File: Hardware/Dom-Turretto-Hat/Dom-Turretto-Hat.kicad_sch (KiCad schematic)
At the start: 4 parts

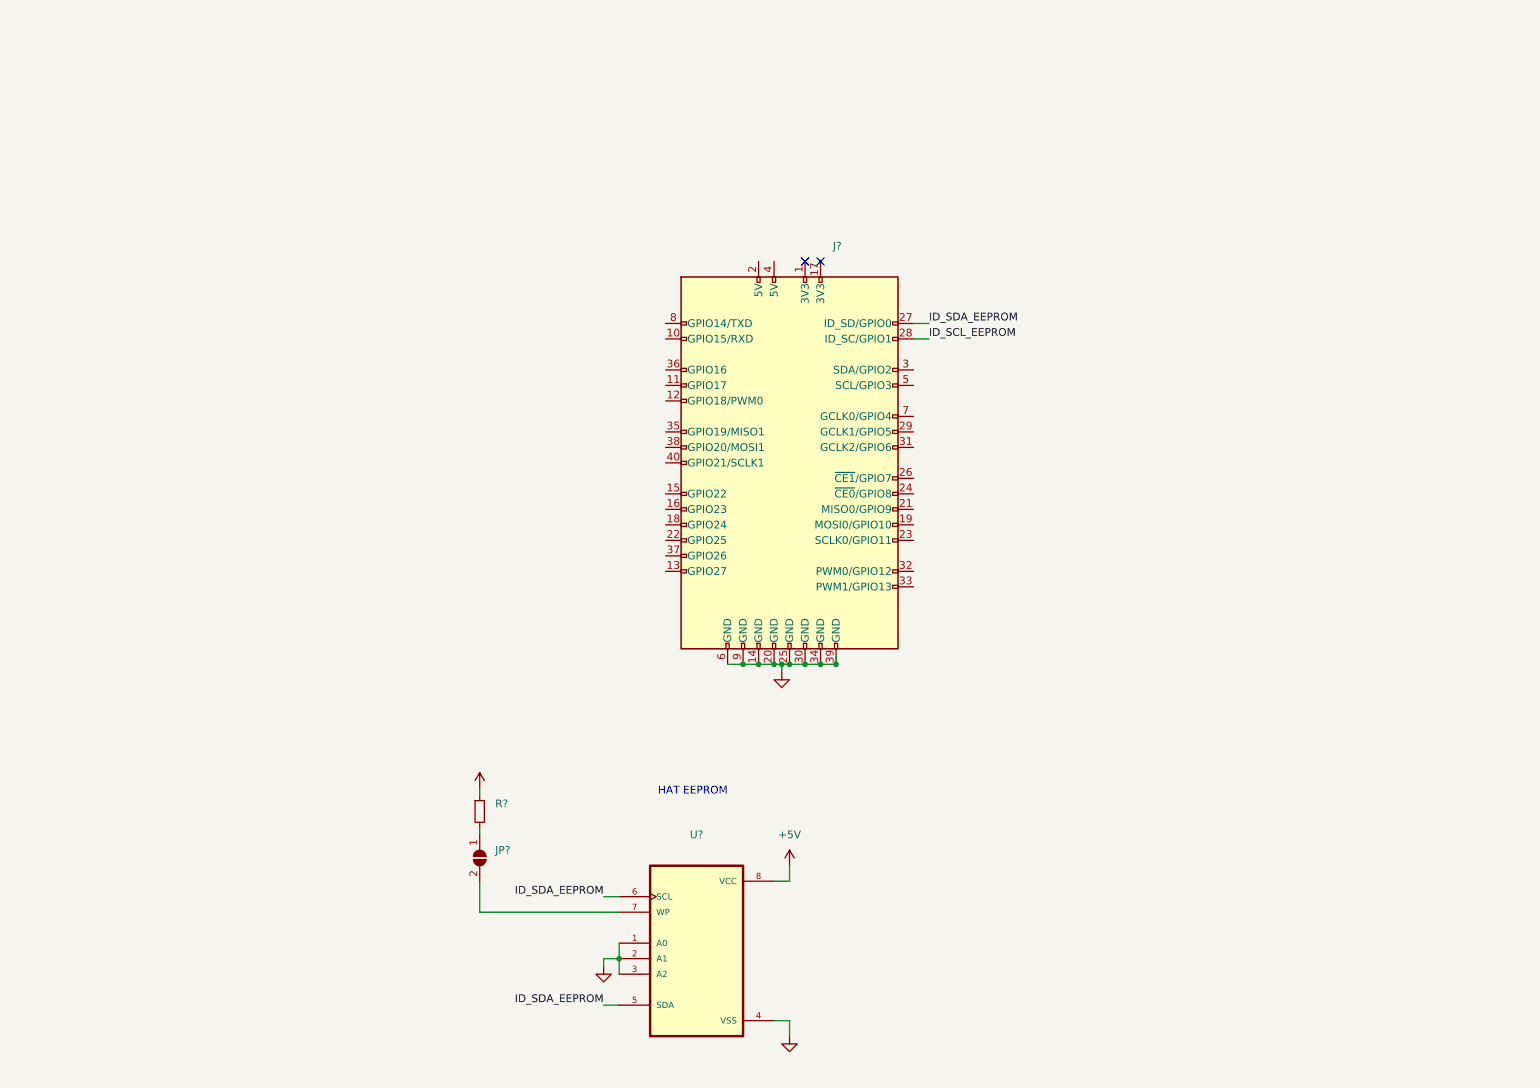
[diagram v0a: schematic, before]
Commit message: Add GPS
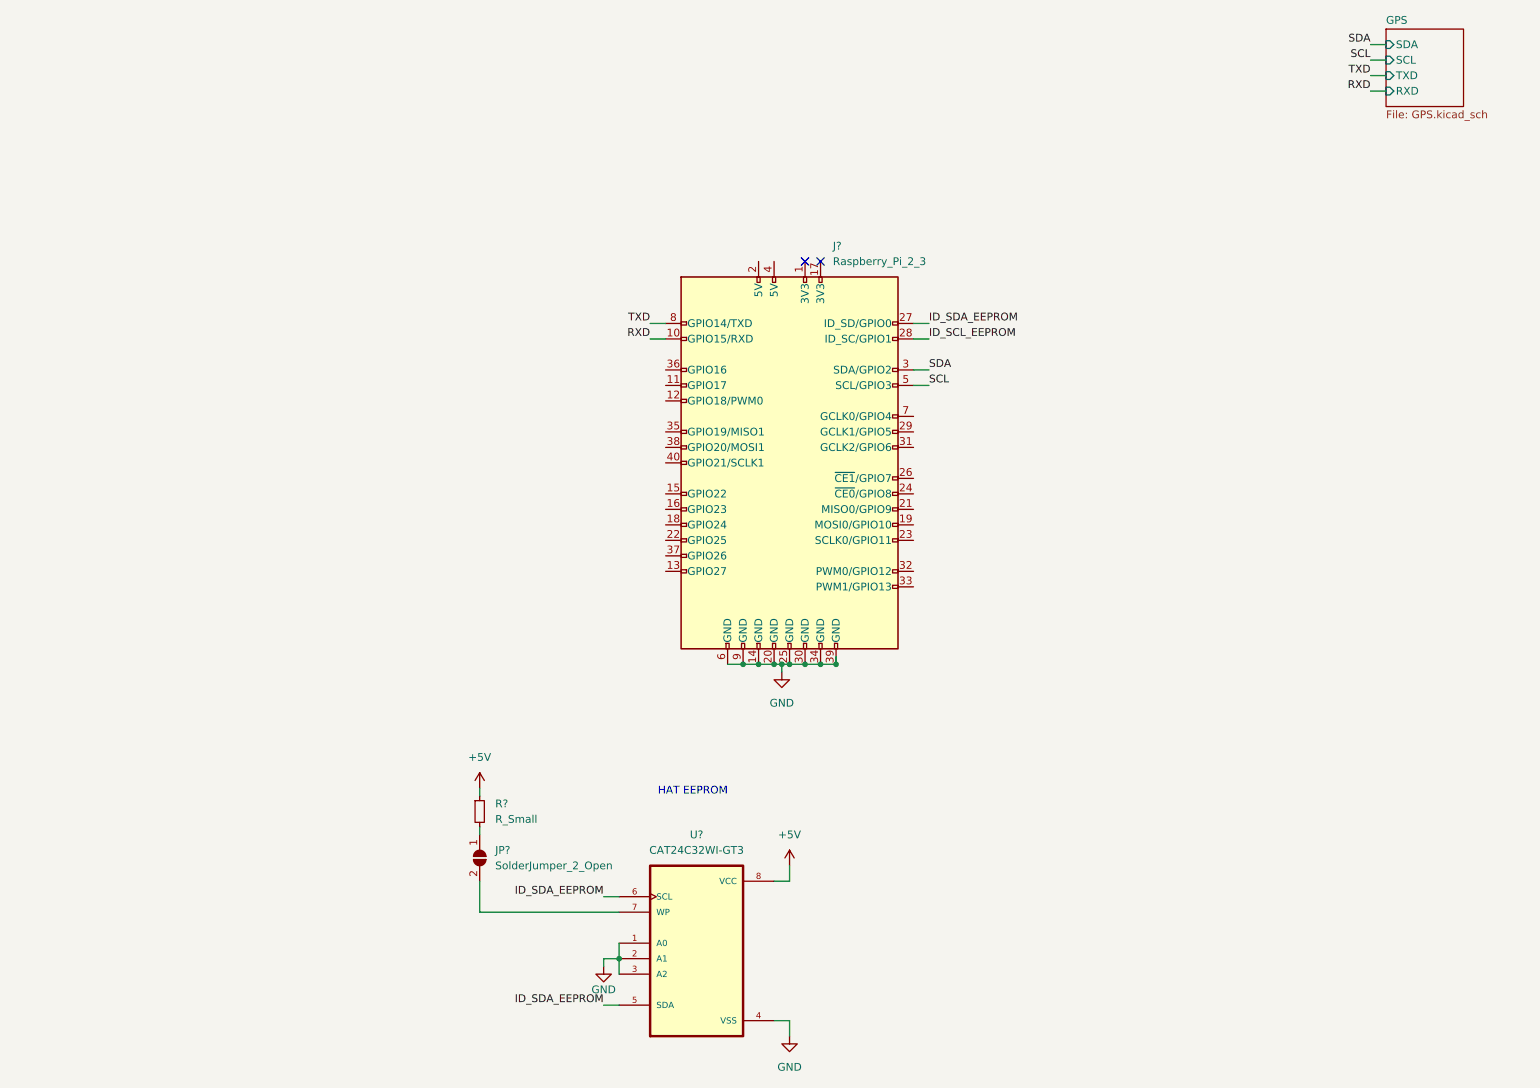
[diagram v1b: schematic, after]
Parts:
- J?: value (none) -> Raspberry_Pi_2_3; footprint (none) -> Connector_PinSocket_2.54mm:PinSocket_2x20_P2.54mm_Vertical
- JP?: value (none) -> SolderJumper_2_Open
- R?: value (none) -> R_Small
- U?: value (none) -> CAT24C32WI-GT3; footprint (none) -> SOIC127P600X175-8N
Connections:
- net RXD: now reaches J?.10 (GPIO15/RXD)
- net SDA: now reaches J?.3 (SDA/GPIO2)
- net SCL: now reaches J?.5 (SCL/GPIO3)
- net TXD: now reaches J?.8 (GPIO14/TXD)
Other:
- added sheet GPS (GPS.kicad_sch)
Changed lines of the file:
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@@
+    (stroke (width 0) (type default) (color 0 0 0 0))
+  )
+  (wire (pts (xy 248.92 30.48) (xy 251.46 30.48))
     (stroke (width 0) (type default) (color 0 0 0 0))
   )
@@
     (stroke (width 0) (type default) (color 0 0 0 0))
   )
+  (wire (pts (xy 130.81 73.66) (xy 133.35 73.66))
+    (stroke (width 0) (type default) (color 0 0 0 0))
+  )
   (wire (pts (xy 173.99 76.2) (xy 176.53 76.2))
     (stroke (width 0) (type default) (color 0 0 0 0))
@@
     (stroke (width 0) (type default) (color 0 0 0 0))
   )
+  (wire (pts (xy 173.99 83.82) (xy 176.53 83.82))
+    (stroke (width 0) (type default) (color 0 0 0 0))
+  )
+  (wire (pts (xy 248.92 27.94) (xy 251.46 27.94))
+    (stroke (width 0) (type default) (color 0 0 0 0))
+  )
   (wire (pts (xy 151.13 187.96) (xy 153.67 187.96))
     (stroke (width 0) (type default) (color 0 0 0 0))
   )
+  (wire (pts (xy 130.81 76.2) (xy 133.35 76.2))
+    (stroke (width 0) (type default) (color 0 0 0 0))
+  )
   (wire (pts (xy 123.19 177.8) (xy 123.19 179.07))
     (stroke (width 0) (type default) (color 0 0 0 0))
@@
     (stroke (width 0) (type default) (color 0 0 0 0))
   )
+  (wire (pts (xy 248.92 35.56) (xy 251.46 35.56))
+    (stroke (width 0) (type default) (color 0 0 0 0))
+  )
   (wire (pts (xy 102.87 165.1) (xy 102.87 170.18))
     (stroke (width 0) (type default) (color 0 0 0 0))
@@
     (stroke (width 0) (type default) (color 0 0 0 0))
   )
+  (wire (pts (xy 173.99 81.28) (xy 176.53 81.28))
+    (stroke (width 0) (type default) (color 0 0 0 0))
+  )
   (wire (pts (xy 173.99 73.66) (xy 176.53 73.66))
     (stroke (width 0) (type default) (color 0 0 0 0))
   )
   (wire (pts (xy 153.67 187.96) (xy 153.67 190.5))
+    (stroke (width 0) (type default) (color 0 0 0 0))
+  )
+  (wire (pts (xy 248.92 33.02) (xy 251.46 33.02))
     (stroke (width 0) (type default) (color 0 0 0 0))
   )
@@
     (effects (font (size 1.27 1.27)) (justify left bottom))
   )
+  (label "SDA" (at 176.53 81.28 0)
+    (effects (font (size 1.27 1.27)) (justify left bottom))
+  )
+  (label "TXD" (at 248.92 33.02 180)
+    (effects (font (size 1.27 1.27)) (justify right bottom))
+  )
   (label "ID_SDA_EEPROM" (at 176.53 73.66 0)
     (effects (font (size 1.27 1.27)) (justify left bottom))
   )
+  (label "SDA" (at 248.92 27.94 180)
+    (effects (font (size 1.27 1.27)) (justify right bottom))
+  )
   (label "ID_SDA_EEPROM" (at 123.19 167.64 180)
     (effects (font (size 1.27 1.27)) (justify right bottom))
   )
+  (label "SCL" (at 176.53 83.82 0)
+    (effects (font (size 1.27 1.27)) (justify left bottom))
+  )
   (label "ID_SDA_EEPROM" (at 123.19 185.42 180)
     (effects (font (size 1.27 1.27)) (justify right bottom))
   )
+  (label "RXD" (at 248.92 35.56 180)
+    (effects (font (size 1.27 1.27)) (justify right bottom))
+  )
+  (label "TXD" (at 130.81 73.66 180)
+    (effects (font (size 1.27 1.27)) (justify right bottom))
+  )
+  (label "RXD" (at 130.81 76.2 180)
+    (effects (font (size 1.27 1.27)) (justify right bottom))
+  )
+  (label "SCL" (at 248.92 30.48 180)
+    (effects (font (size 1.27 1.27)) (justify right bottom))
+  )
   (symbol (lib_id "power:GND") (at 152.4 130.81 0) (unit 1)
     (in_bom yes) (on_board yes) (fields_autoplaced)
@@
       (effects (font (size 1.27 1.27)) hide)
     )
-    (property "Value" "" (id 1) (at 152.4 135.89 0))
+    (property "Value" "GND" (id 1) (at 152.4 135.89 0))
     (property "Footprint" "" (id 2) (at 152.4 130.81 0)
       (effects (font (size 1.27 1.27)) hide)
@@
     (in_bom yes) (on_board yes) (fields_autoplaced)
     (property "Reference" "U?" (id 0) (at 138.43 157.48 0))
-    (property "Value" "" (id 1) (at 138.43 160.02 0))
-    (property "Footprint" "" (id 2) (at 138.43 175.26 0)
+    (property "Value" "CAT24C32WI-GT3" (id 1) (at 138.43 160.02 0))
+    (property "Footprint" "SOIC127P600X175-8N" (id 2) (at 138.43 175.26 0)
       (effects (font (size 1.27 1.27)) (justify left bottom) hide)
     )
@@
       (effects (font (size 1.27 1.27)) hide)
     )
-    (property "Value" "" (id 1) (at 102.87 144.78 0))
+    (property "Value" "+5V" (id 1) (at 102.87 144.78 0))
     (property "Footprint" "" (id 2) (at 102.87 149.86 0)
       (effects (font (size 1.27 1.27)) hide)
@@
       (effects (font (size 1.27 1.27)) (justify left))
     )
-    (property "Value" "" (id 1) (at 160.7694 63.5 0)
-      (effects (font (size 1.27 1.27)) (justify left))
-    )
-    (property "Footprint" "" (id 2) (at 153.67 96.52 0)
+    (property "Value" "Raspberry_Pi_2_3" (id 1) (at 160.7694 63.5 0)
+      (effects (font (size 1.27 1.27)) (justify left))
+    )
+    (property "Footprint" "Connector_PinSocket_2.54mm:PinSocket_2x20_P2.54mm_Vertical" (id 2) (at 153.67 96.52 0)
       (effects (font (size 1.27 1.27)) hide)
     )
@@
       (effects (font (size 1.27 1.27)) (justify left))
     )
-    (property "Value" "" (id 1) (at 105.41 162.5599 90)
+    (property "Value" "SolderJumper_2_Open" (id 1) (at 105.41 162.5599 90)
       (effects (font (size 1.27 1.27)) (justify left))
     )
@@
       (effects (font (size 1.27 1.27)) hide)
     )
-    (property "Value" "" (id 1) (at 153.67 195.58 0))
+    (property "Value" "GND" (id 1) (at 153.67 195.58 0))
     (property "Footprint" "" (id 2) (at 153.67 190.5 0)
       (effects (font (size 1.27 1.27)) hide)
@@
       (effects (font (size 1.27 1.27)) hide)
     )
-    (property "Value" "" (id 1) (at 123.19 182.88 0))
+    (property "Value" "GND" (id 1) (at 123.19 182.88 0))
     (property "Footprint" "" (id 2) (at 123.19 179.07 0)
       (effects (font (size 1.27 1.27)) hide)
@@
       (effects (font (size 1.27 1.27)) (justify left))
     )
-    (property "Value" "" (id 1) (at 105.41 154.9399 0)
+    (property "Value" "R_Small" (id 1) (at 105.41 154.9399 0)
       (effects (font (size 1.27 1.27)) (justify left))
     )
@@
     (pin "1")
     (pin "2")
+  )
+  (sheet (at 251.46 25.4) (size 12.7 12.7) (fields_autoplaced)
+    (stroke (width 0.1524) (type solid) (color 0 0 0 0))
+    (fill (color 0 0 0 0.0000))
+    (property "Sheet name" "GPS" (id 0) (at 251.46 24.6884 0)
+      (effects (font (size 1.27 1.27)) (justify left bottom))
+    )
+    (property "Sheet file" "GPS.kicad_sch" (id 1) (at 251.46 38.6846 0)
+      (effects (font (size 1.27 1.27)) (justify left top))
+    )
+    (pin "RXD" input (at 251.46 35.56 180)
+      (effects (font (size 1.27 1.27)) (justify left))
+    )
+    (pin "SDA" input (at 251.46 27.94 180)
+      (effects (font (size 1.27 1.27)) (justify left))
+    )
+    (pin "SCL" input (at 251.46 30.48 180)
+      (effects (font (size 1.27 1.27)) (justify left))
+    )
+    (pin "TXD" input (at 251.46 33.02 180)
+      (effects (font (size 1.27 1.27)) (justify left))
+    )
   )
   (sheet_instances
     (path "/" (page "1"))
+    (path "/c8c14f7c-55ef-44f2-9b65-a499409017e1" (page "2"))
   )
   (symbol_instances
@@
       (reference "#PWR?") (unit 1) (value "GND") (footprint "")
     )
+    (path "/c8c14f7c-55ef-44f2-9b65-a499409017e1/451985fb-27af-4988-a96b-5b9018357ef6"
+      (reference "#PWR?") (unit 1) (value "GND") (footprint "")
+    )
     (path "/4bc4c433-f063-4f06-891b-84c21537146f"
       (reference "#PWR?") (unit 1) (value "+5V") (footprint "")
     )
+    (path "/c8c14f7c-55ef-44f2-9b65-a499409017e1/899f9b0d-851b-40b2-95d9-0bf4320cfc7f"
+      (reference "#PWR?") (unit 1) (value "+3V3") (footprint "")
+    )
     (path "/ba4a3115-885a-4dd4-8dfa-d43bc604d1e0"
       (reference "#PWR?") (unit 1) (value "+5V") (footprint "")
     )
+    (path "/c8c14f7c-55ef-44f2-9b65-a499409017e1/d58204f5-4242-4763-8399-6e93946856c1"
+      (reference "#PWR?") (unit 1) (value "GND") (footprint "")
+    )
     (path "/d76951c7-90df-44ef-9dcf-7210c88290e4"
       (reference "#PWR?") (unit 1) (value "GND") (footprint "")
@@
       (reference "#PWR?") (unit 1) (value "GND") (footprint "")
     )
+    (path "/c8c14f7c-55ef-44f2-9b65-a499409017e1/e4566a45-8e06-47ea-a935-fa62dd278c90"
+      (reference "#PWR?") (unit 1) (value "+3V3") (footprint "")
+    )
+    (path "/c8c14f7c-55ef-44f2-9b65-a499409017e1/4fb87244-379d-4e75-94c2-9521bcc0ec81"
+      (reference "C?") (unit 1) (value "10nF") (footprint "Capacitor_SMD:C_0603_1608Metric")
+    )
     (path "/61fae217-e18a-4e68-8630-42cc06a8ba2f"
       (reference "J?") (unit 1) (value "Raspberry_Pi_2_3") (footprint "Connector_PinSocket_2.54mm:PinSocket_2x20_P2.54mm_Vertical")
     )
+    (path "/c8c14f7c-55ef-44f2-9b65-a499409017e1/6a180251-fad0-4435-9a6c-41f5e820bcf1"
+      (reference "J?") (unit 1) (value "Conn_Coaxial") (footprint "Connector_Coaxial:SMA_Molex_73251-1153_EdgeMount_Horizontal")
+    )
     (path "/a4265e2c-06a9-41da-b42d-91d87bbe6b18"
       (reference "JP?") (unit 1) (value "SolderJumper_2_Open") (footprint "")
     )
+    (path "/c8c14f7c-55ef-44f2-9b65-a499409017e1/d6c763e2-1952-4281-9868-501fafa3b154"
+      (reference "L?") (unit 1) (value "27nH") (footprint "Inductor_SMD:L_0603_1608Metric")
+    )
+    (path "/c8c14f7c-55ef-44f2-9b65-a499409017e1/8a505506-ea00-4e73-916e-6375c9e26bd9"
+      (reference "R?") (unit 1) (value "10") (footprint "Resistor_SMD:R_0603_1608Metric")
+    )
+    (path "/c8c14f7c-55ef-44f2-9b65-a499409017e1/d53051b6-ebe9-4558-9887-00e35561baeb"
+      (reference "R?") (unit 1) (value "10K") (footprint "Resistor_SMD:R_0603_1608Metric")
+    )
     (path "/e3cbd370-7c22-4222-878e-9ad9b35baaf2"
       (reference "R?") (unit 1) (value "R_Small") (footprint "")
@@
       (reference "U?") (unit 1) (value "CAT24C32WI-GT3") (footprint "SOIC127P600X175-8N")
     )
-  )
+    (path "/c8c14f7c-55ef-44f2-9b65-a499409017e1/5c054c83-012c-4e45-901b-5550fc59a449"
+      (reference "U?") (unit 1) (value "MAX-M8Q") (footprint "RF_GPS:ublox_MAX")
+    )
+  )

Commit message: Add power circuitry
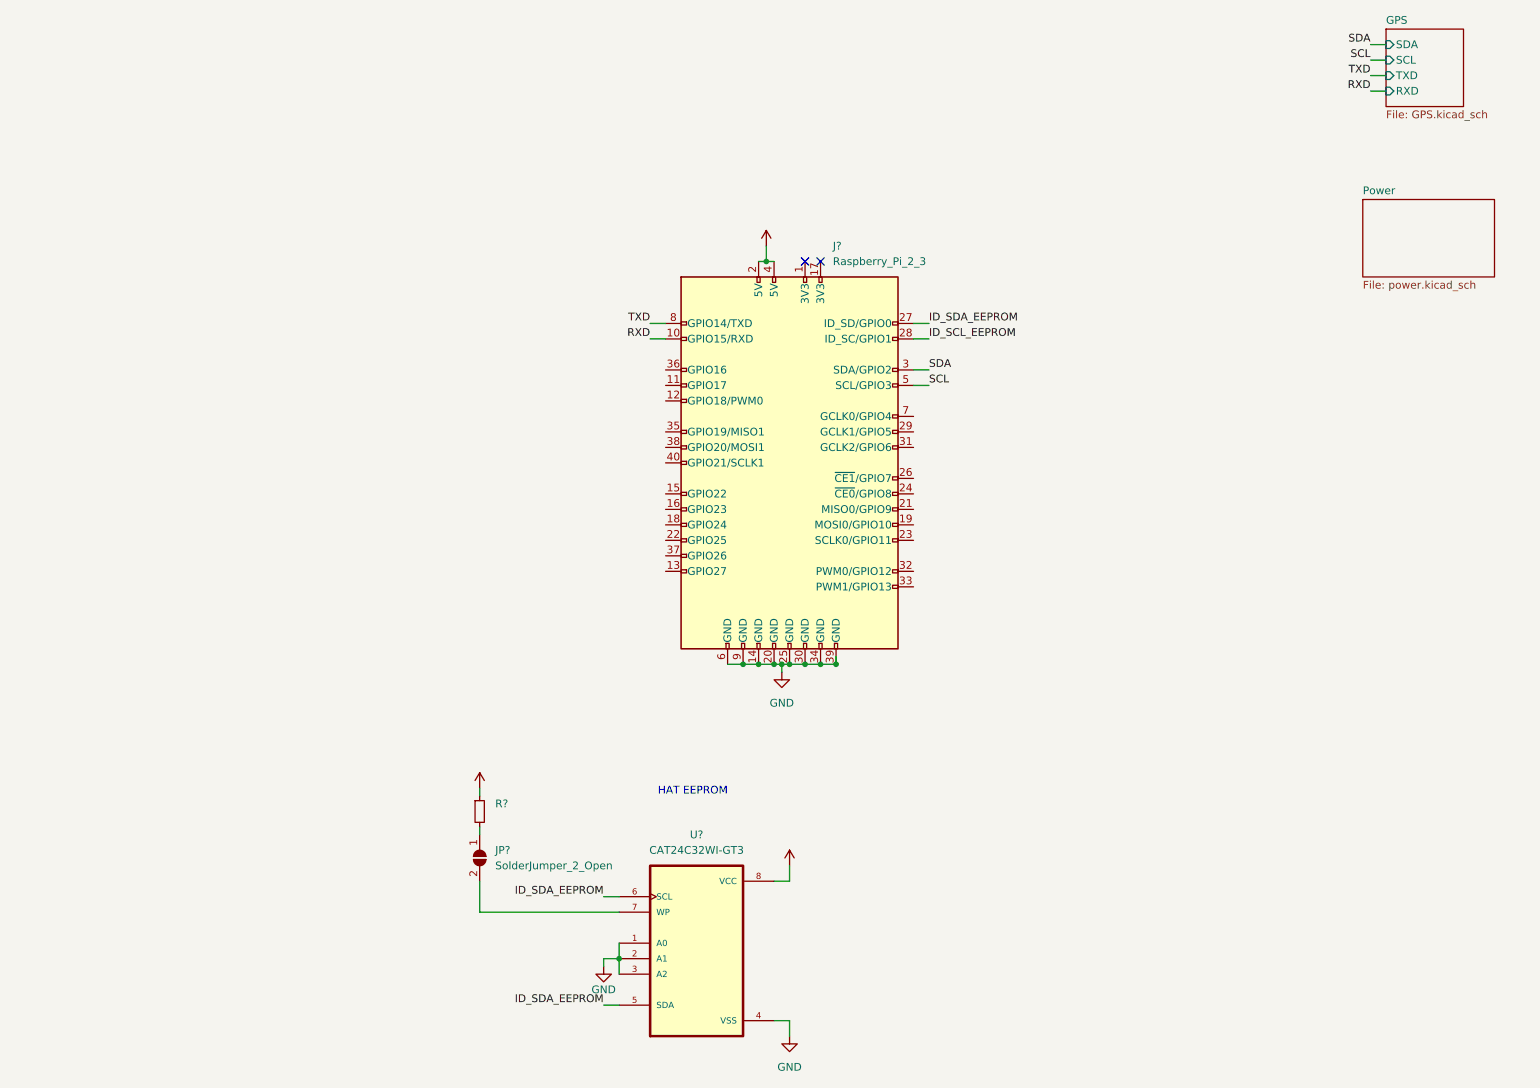
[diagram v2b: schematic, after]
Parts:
- R?: value R_Small -> (none)
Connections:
- net +5V: now also J?.2 (5V), J?.4 (5V); no longer R?.1, U?.8 (VCC)
- new net +3V3: R?.1, U?.8 (VCC)
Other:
- added sheet Power (power.kicad_sch)
